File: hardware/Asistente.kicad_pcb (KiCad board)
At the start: 2 copper layers, 66.7 x 92.1 mm, 7 parts, among them U2 pam8403

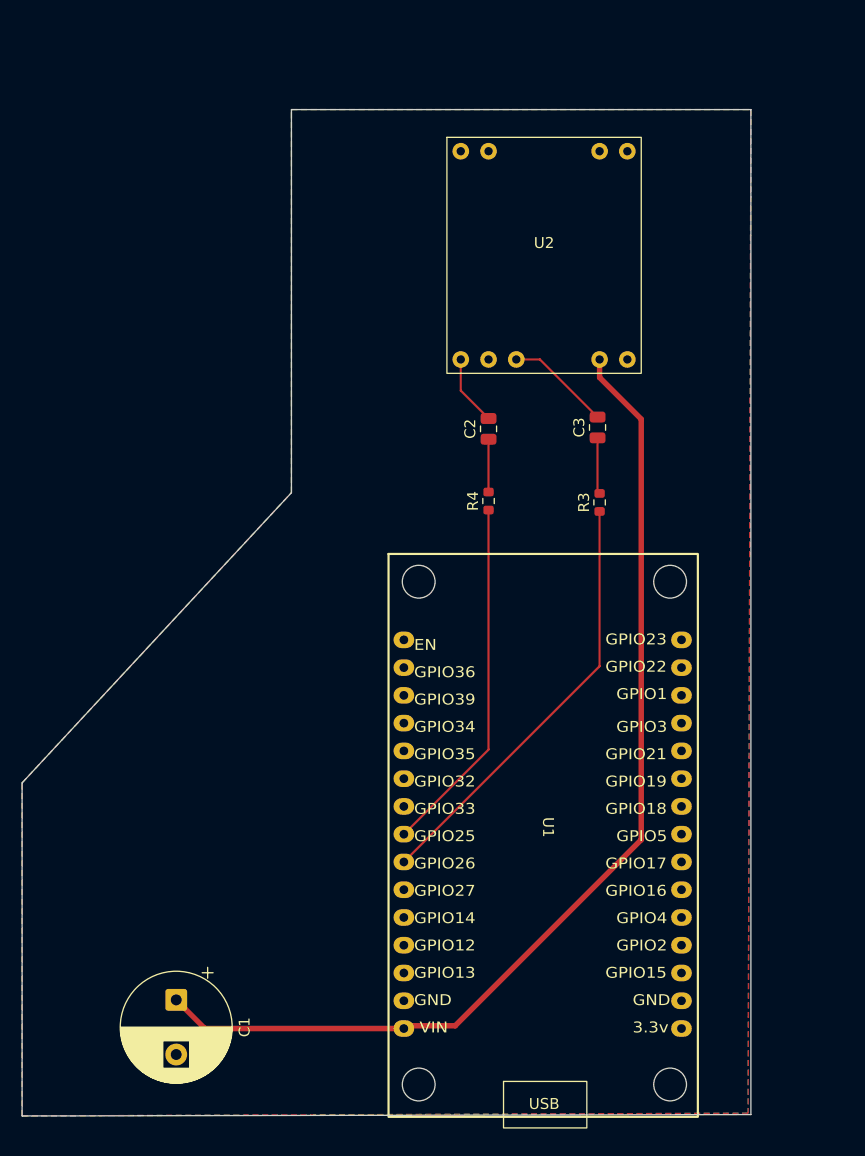
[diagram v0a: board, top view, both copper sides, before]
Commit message: feat: add external connectors for OLED, mic and speakers, update gerber files
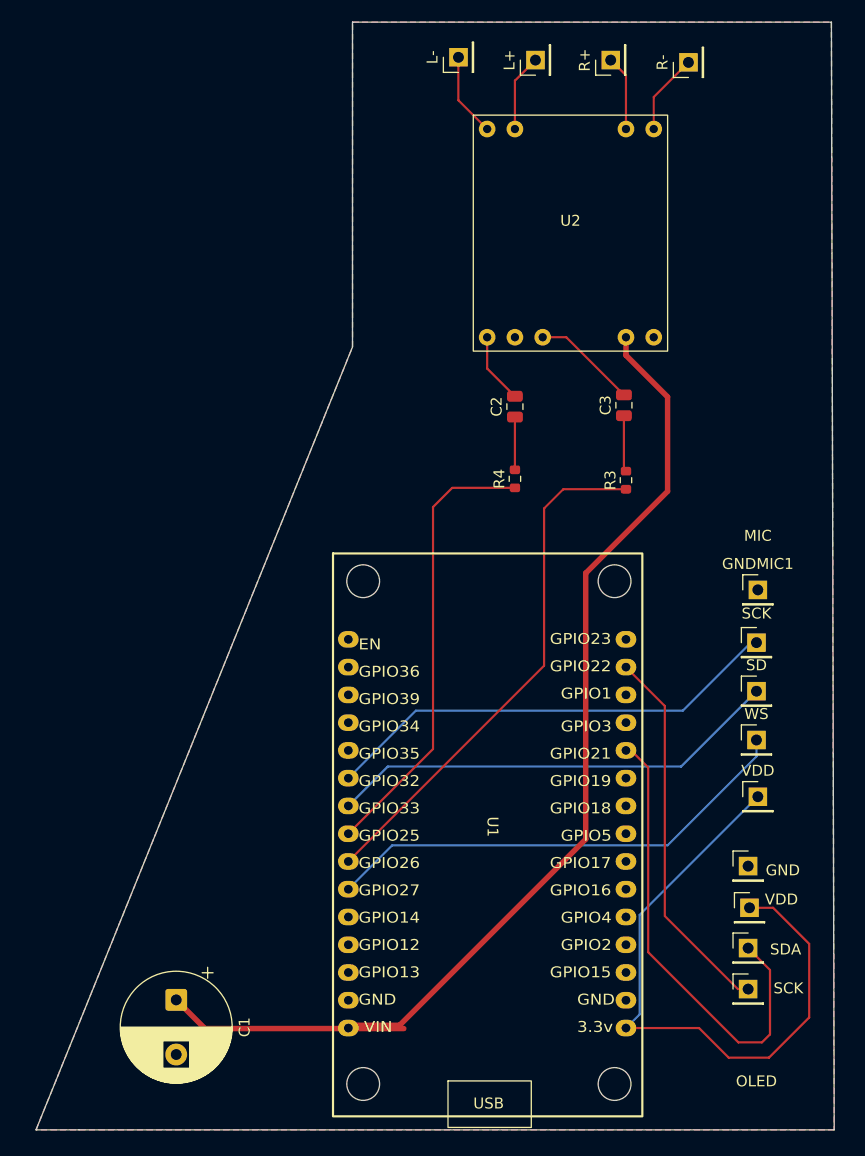
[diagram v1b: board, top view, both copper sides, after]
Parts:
- added GND: Conn_01x01_Pin, Connector_PinHeader_2.54mm:PinHeader_1x01_P2.54mm_Vertical, F.Cu at (164.3, 102.5)
- added GNDMIC1: Conn_01x01_Pin, Connector_PinHeader_2.54mm:PinHeader_1x01_P2.54mm_Vertical, F.Cu at (165.2, 77.2)
- added L+: Conn_01x01_Pin, Connector_PinHeader_2.54mm:PinHeader_1x01_P2.54mm_Vertical, F.Cu at (144.9, 28.7)
- added L-: Conn_01x01_Pin, Connector_PinHeader_2.54mm:PinHeader_1x01_P2.54mm_Vertical, F.Cu at (137.8, 28.5)
- added R+: Conn_01x01_Pin, Connector_PinHeader_2.54mm:PinHeader_1x01_P2.54mm_Vertical, F.Cu at (151.8, 28.7)
- added R-: Conn_01x01_Pin, Connector_PinHeader_2.54mm:PinHeader_1x01_P2.54mm_Vertical, F.Cu at (158.9, 29.0)
- added SCK: Conn_01x01_Pin, Connector_PinHeader_2.54mm:PinHeader_1x01_P2.54mm_Vertical, F.Cu at (165.1, 82.0)
- added SCK: Conn_01x01_Pin, Connector_PinHeader_2.54mm:PinHeader_1x01_P2.54mm_Vertical, F.Cu at (164.3, 113.7)
- added SD: Conn_01x01_Pin, Connector_PinHeader_2.54mm:PinHeader_1x01_P2.54mm_Vertical, F.Cu at (165.1, 86.5)
- added SDA: Conn_01x01_Pin, Connector_PinHeader_2.54mm:PinHeader_1x01_P2.54mm_Vertical, F.Cu at (164.3, 110.0)
- added VDD: Conn_01x01_Pin, Connector_PinHeader_2.54mm:PinHeader_1x01_P2.54mm_Vertical, F.Cu at (164.5, 106.3)
- added VDD: Conn_01x01_Pin, Connector_PinHeader_2.54mm:PinHeader_1x01_P2.54mm_Vertical, F.Cu at (165.2, 96.1)
- added WS: Conn_01x01_Pin, Connector_PinHeader_2.54mm:PinHeader_1x01_P2.54mm_Vertical, F.Cu at (165.1, 91.0)
- C2, C3: value 10uf -> 100nf
- R3: value 100 -> 1k
- R4: value 100Ω -> 1k
- moved U1 5.08 mm to (139.7, 100.3)
- moved C2 3.15 mm to (143.0, 60.5)
- moved R3 3.15 mm to (153.2, 67.2)
- moved R4 3.15 mm to (143.0, 67.1)
- moved C3 3.15 mm to (153.0, 60.3)
- moved U2 3.15 mm to (148.1, 43.9)
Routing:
- net Net-(DS1-VDD): track 0.00 -> 59.1 mm
- net Net-(J11-Pin_1): track 0.00 -> 43.9 mm
- net Net-(DS1-SDA): track 0.00 -> 43.2 mm
- net Net-(J10-Pin_1): track 0.00 -> 42.5 mm
- net Net-(J9-Pin_1): track 0.00 -> 41.7 mm
- net Net-(DS1-SCK): track 0.00 -> 34.6 mm
- net Net-(U1-GPIO25): track 33.1 -> 41.3 mm
- net Net-(U1-GPIO26): track 39.7 -> 47.9 mm
- net Net-(J5-Pin_1): track 0.00 -> 7.89 mm
- net Net-(J7-Pin_1): track 0.00 -> 7.41 mm
- net Net-(J6-Pin_1): track 0.00 -> 7.08 mm
- net Net-(J8-Pin_1): track 0.00 -> 6.88 mm
- net +5V: track 96.3 -> 101.4 mm
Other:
- board size 66.7 x 92.1 mm -> 73 x 101.3 mm
- board text added: "MIC"
- board text added: "OLED"

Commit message: Refactor and remove obsolete files
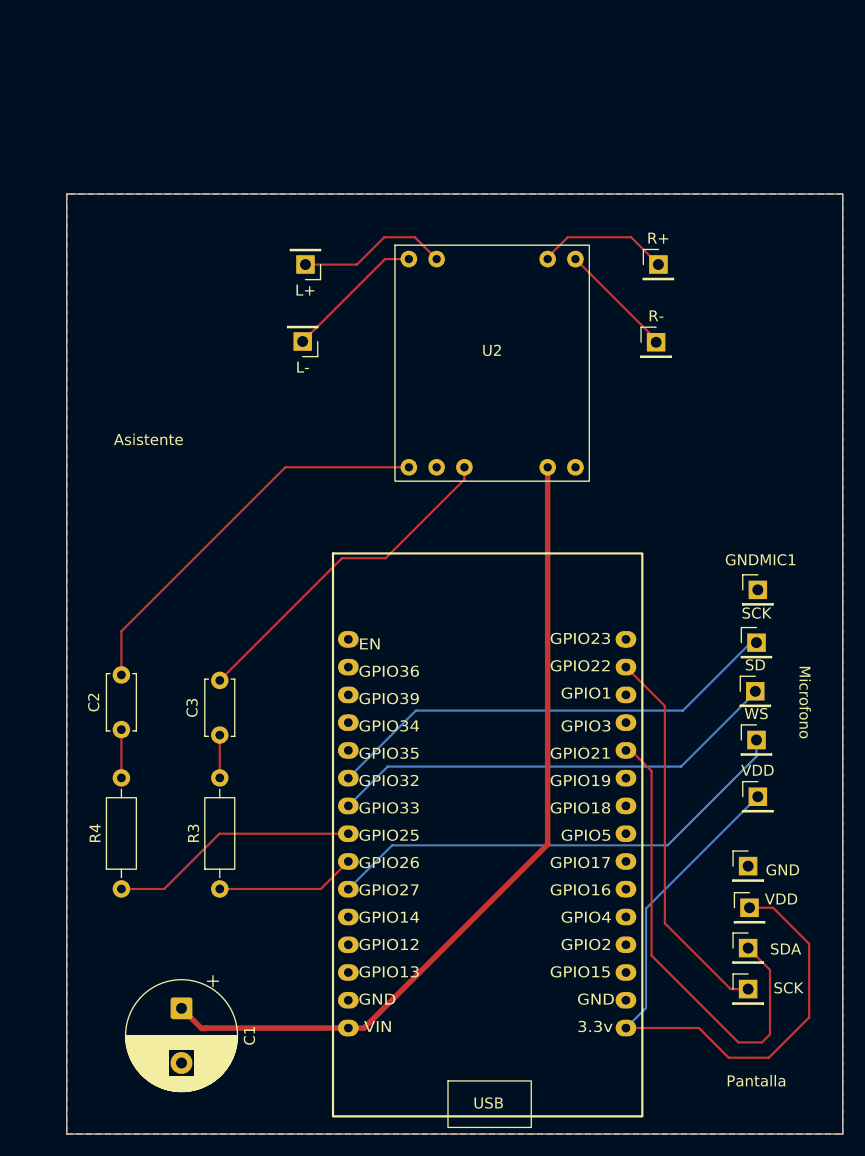
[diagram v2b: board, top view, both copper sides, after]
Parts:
- C2, C3: footprint Capacitor_SMD:C_0805_2012Metric -> Capacitor_THT:C_Disc_D5.0mm_W2.5mm_P5.00mm
- R3, R4: footprint Resistor_SMD:R_0603_1608Metric -> Resistor_THT:R_Axial_DIN0207_L6.3mm_D2.5mm_P10.16mm_Horizontal
- moved R3 52.7 mm to (116.0, 104.6)
- moved R4 52.0 mm to (107.0, 104.6)
- moved C3 47.7 mm to (116.0, 90.5)
- moved C2 46.6 mm to (107.0, 90.0)
- moved L- 29.7 mm to (123.6, 54.5), turned to 180 degrees
- moved L+ 28.2 mm to (123.8, 47.5), turned to 180 degrees
- moved R- 25.8 mm to (155.9, 54.6), turned to 0 degrees
- moved R+ 19.2 mm to (156.1, 47.5), turned to 0 degrees
- moved U2 13.9 mm to (140.9, 55.8)
- moved C1 0.91 mm to (112.5, 115.5)
- moved SD 0.10 mm to (165.0, 86.5)
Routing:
- net Net-(U1-GPIO26): track 47.9 -> 12.8 mm
- net Net-(U2-L): track 6.45 -> 36.5 mm
- net +5V: track 101.4 -> 75.7 mm
- net Net-(U2-R): track 9.62 -> 31.1 mm
- net Net-(U1-GPIO25): track 41.3 -> 22.9 mm
- net Net-(J6-Pin_1): track 7.08 -> 13.9 mm
- net Net-(J8-Pin_1): track 6.88 -> 12.1 mm
- net Net-(J5-Pin_1): track 7.89 -> 12.8 mm
- net Net-(J7-Pin_1): track 7.41 -> 10.7 mm
- net Net-(C3-Pad1): track 5.39 -> 3.92 mm
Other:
- board size 73 x 101.3 mm -> 71 x 86 mm
- board text added: "Asistente"
- board text added: "Microfono"
- board text added: "Pantalla"
- board text removed: "MIC"
- board text removed: "OLED"
